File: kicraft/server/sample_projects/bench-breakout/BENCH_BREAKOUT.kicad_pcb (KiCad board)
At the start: 2 copper layers, 47.5 x 36.6 mm, 16 parts, among them J1 USB-C Receptacle, Q1 AO3401A, U1 USBLC6-2SC6, U2 AMS1117-3.3

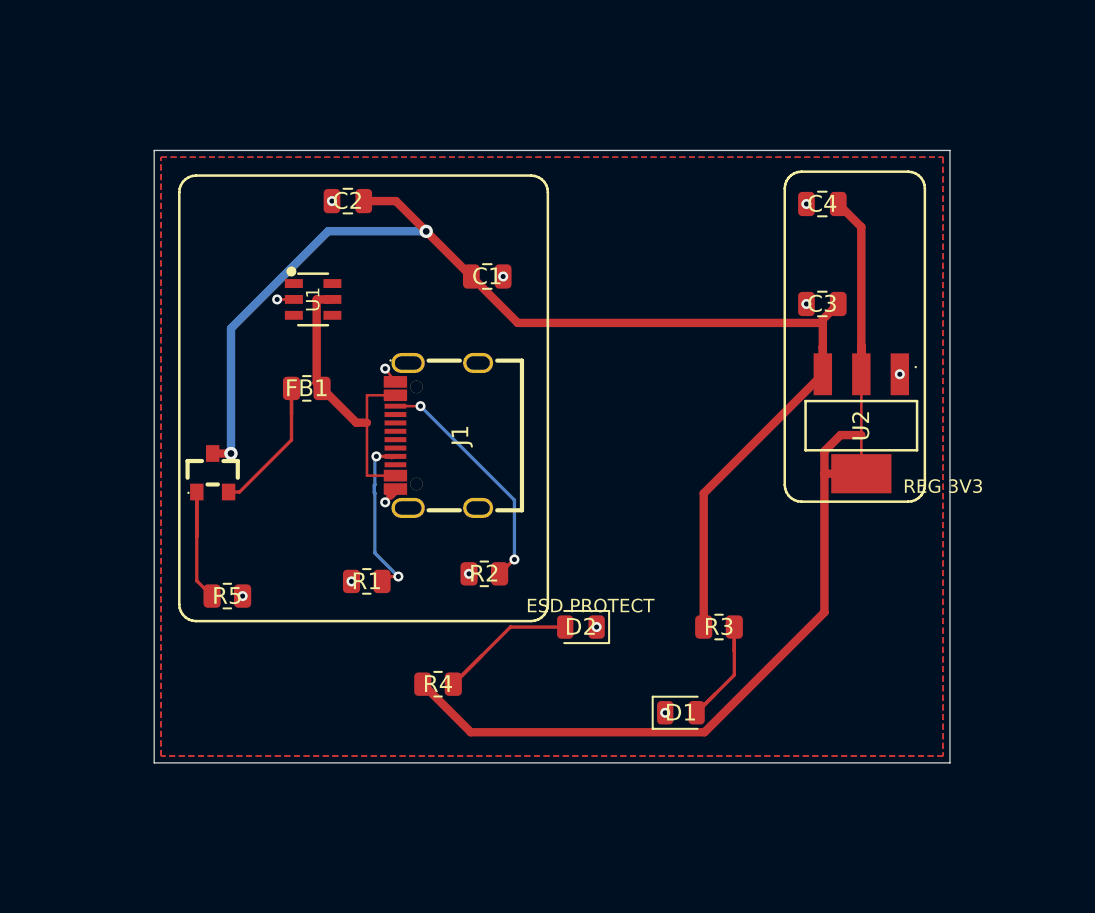
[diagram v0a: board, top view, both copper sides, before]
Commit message: feat(showcase): refresh landing samples from self-eval 20260614
Promote the three best boards from self-eval batch 20260614T215540Z
(all grade B) into the landing-page showcase, replacing the regressed
PIR night light (D/45, hit erc_errors + unprogrammable_mcu gates):

- usb-pd-trigger (NEW, featured hero) — 81.0, fab-ready
- weather-sensor (re-promoted; stem A_BMP280_BAROMETRIC -> BMP280_QWIIC_USB_C)
- bench-breakout (re-promoted; 4->5 sheets, 16->19 parts)

Regenerated board.png/hero.png renders and interactive board.glb models
via scripts/promote_to_sample.py. Already live (deploy/restart-web.sh).

Co-Authored-By: Claude Opus 4.8 (1M context) <noreply@anthropic.com>
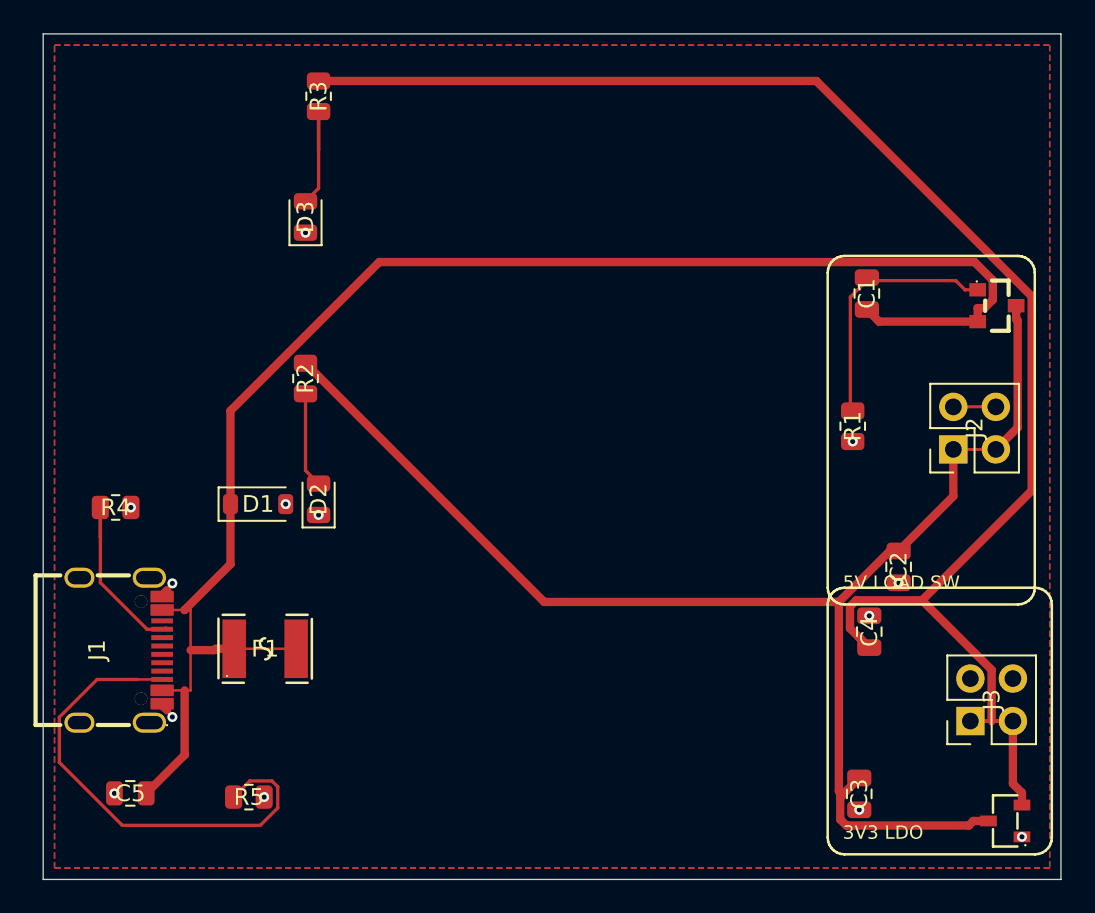
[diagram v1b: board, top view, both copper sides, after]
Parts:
- removed FB1: 600R @ 100MHz, R_0805_2012Metric
- removed U2: AMS1117-3.3, SOT-223-3_L6.5-W3.4-P2.30-LS7.0-BR
- added C5: 10uF, C_0805_2012Metric, F.Cu at (123.3, 125.1)
- added D3: Green, LED_0805_2012Metric, F.Cu at (133.8, 90.7)
- added F1: MF-MSMF050-2, F1812, F.Cu at (131.4, 116.5)
- added J2: 2x02 Header, PinHeader_2x02_P2.54mm_Vertical, F.Cu at (172.5, 104.6)
- added J3: 2x02 Header, PinHeader_2x02_P2.54mm_Vertical, F.Cu at (173.5, 120.8)
- C1: value 10Î¼F -> 100nF
- C2: value 0.1Î¼F -> 10uF
- C3, C4: value 10Î¼F -> 1uF
- D1: value Red LED -> 5V TVS; footprint LED_0805_2012Metric -> D_SOD-123
- D2: value Red LED -> Red
- J1: value USB-C Receptacle -> TYPE-C-31-M-12
- R1: value 5.1k -> 100k
- R2: value 5.1k -> 470
- R3: value 1k -> 470
- R4: value 1k -> 5.1k
- R5: value 100k -> 5.1k
- U1: value USBLC6-2SC6 -> XC6206P332MR; footprint SOT-23-6_L2.9-W1.6-P0.95-LS2.8-BL -> SOT-23-3_L2.9-W1.3-P1.90-LS2.4-BR
- moved U1 51.8 mm to (175.6, 126.8), turned to 0 degrees
- moved Q1 47.9 mm to (175.1, 96.0), turned to 180 degrees
- moved R3 39.7 mm to (134.6, 83.5), turned to -90 degrees
- moved C2 39.5 mm to (169.2, 111.6), turned to -90 degrees
- moved R1 30.5 mm to (166.5, 103.2), turned to -90 degrees
- moved C3 29.3 mm to (166.8, 125.1), turned to -90 degrees
- moved D1 28.2 mm to (130.9, 107.8)
- moved C4 25.7 mm to (167.4, 115.5), turned to 90 degrees
- moved J1 22.8 mm to (122.7, 116.6), turned to -90 degrees
- moved C1 22.7 mm to (167.3, 95.3), turned to -90 degrees
- moved R4 22.0 mm to (122.4, 108.0)
- moved D2 17.4 mm to (134.6, 107.5), turned to 90 degrees
- moved R2 15.8 mm to (133.8, 100.3), turned to -90 degrees
- moved R5 12.1 mm to (130.4, 125.3)
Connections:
- C1 pad 1: +5V -> GATE
- C1 pad 2: GND -> VBUS
- D1 pad 1: GND -> VBUS
- D1 pad 2: LED5V -> GND
- D2 pad 2: LED3V3 -> LED5V_ANODE
- Q1 pad 1: GATE_PULL -> GATE
- Q1 pad 2: VUSB -> VBUS
- R1 pad 1: CC1 -> GATE
- R2 pad 1: CC2 -> +5V
- R2 pad 2: GND -> LED5V_ANODE
- R3 pad 1: +5V -> +3V3
- R3 pad 2: LED5V -> LED3V3_ANODE
- R4 pad 1: +3V3 -> CC1
- R4 pad 2: LED3V3 -> GND
- R5 pad 1: GATE_PULL -> CC2
- U1 pad 1: (no net) -> GND
- U1 pad 2: GND -> +3V3
- U1 pad 3: (no net) -> +5V
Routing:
- net VBUS: track 18.1 -> 94.3 mm
- net +3V3: track 61.0 -> 103.9 mm
- net +5V: track 77.5 -> 96.0 mm, vias 2 -> 0
- net GATE: track 0.00 -> 15.3 mm
- net CC2: track 14.8 -> 29.9 mm, vias 2 -> 0
- net LED3V3: track 10.5 -> 0.00 mm
- net GATE_PULL: track 9.89 -> 0.00 mm
- net VUSB: track 9.67 -> 0.00 mm
- net LED5V: track 9.08 -> 0.00 mm
- net LED3V3_ANODE: track 0.00 -> 8.53 mm
- net LED5V_ANODE: track 0.00 -> 5.69 mm
- net GND: track 3.53 -> 8.13 mm
- net CC1: track 10.7 -> 11.3 mm, vias 2 -> 0
- added copper zone on F.Cu, net VBUS
- removed copper zone on F.Cu, net +5V
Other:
- board size 47.5 x 36.6 mm -> 60.8 x 50.5 mm
- board text added: "3V3 LDO"
- board text added: "5V LOAD SW"
- board text removed: "ESD PROTECT"
- board text removed: "REG 3V3"
